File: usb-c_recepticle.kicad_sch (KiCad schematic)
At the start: 4 parts, among them J2 USB_C_Receptacle_USB2.0_16P, U7 USBLC6-2SC6

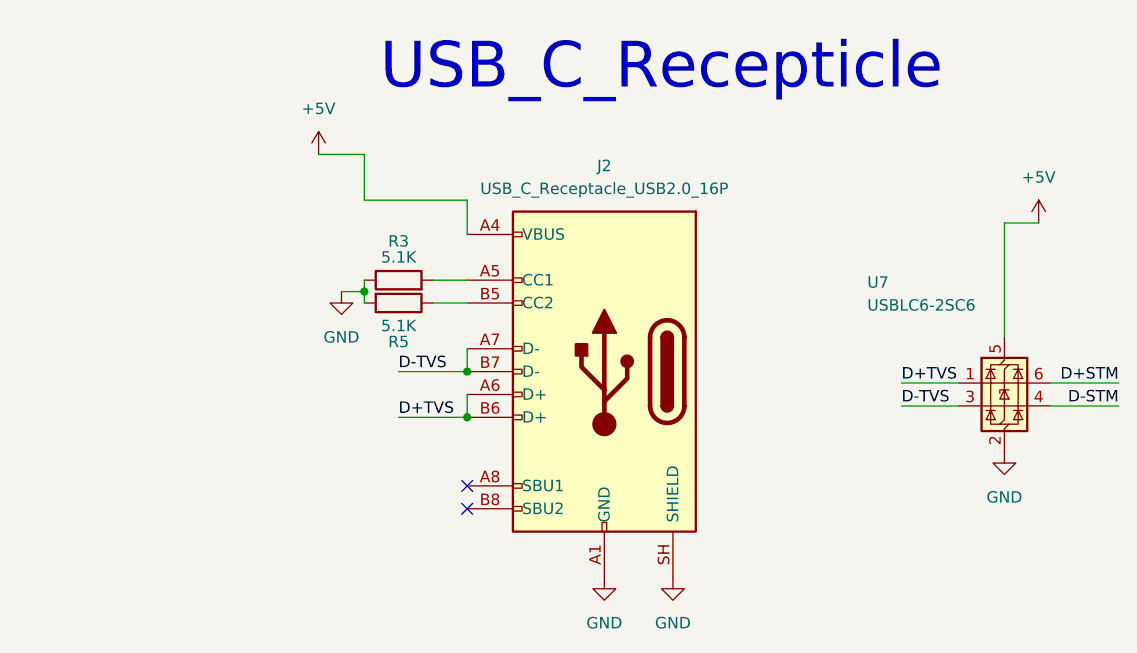
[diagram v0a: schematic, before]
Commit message: Feat: added Canbus
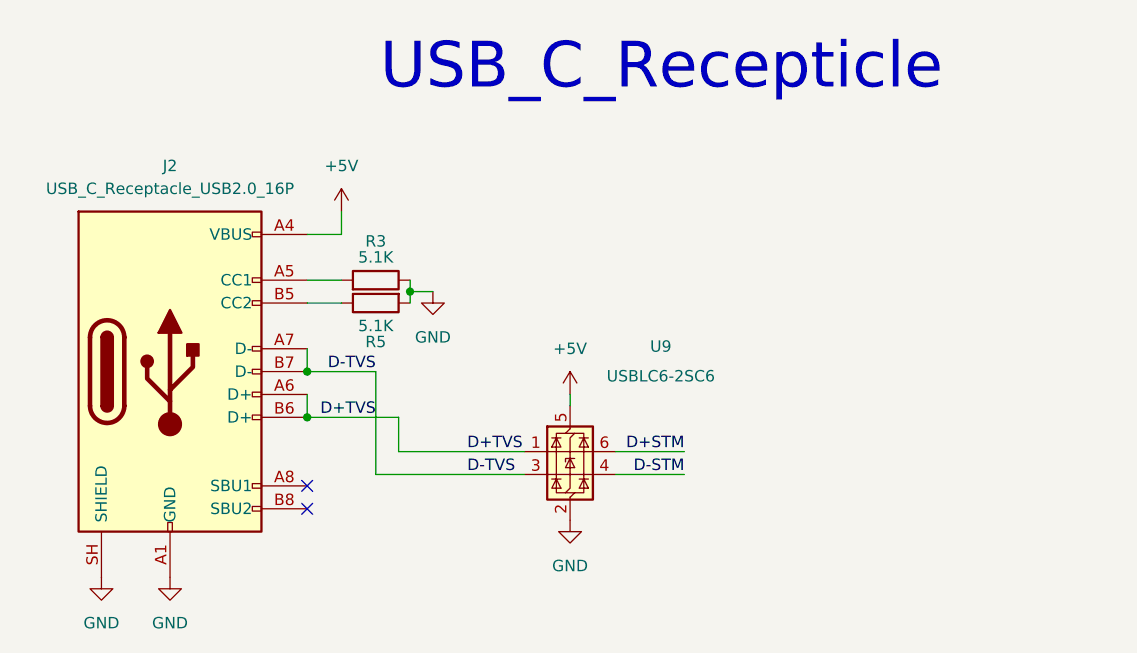
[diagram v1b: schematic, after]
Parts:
- removed U7: USBLC6-2SC6, Package_TO_SOT_SMD:SOT-23-6, symbol Power_Protection:USBLC6-2SC6
- added U9: USBLC6-2SC6, Package_TO_SOT_SMD:SOT-23-6, symbol Power_Protection:USBLC6-2SC6
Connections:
- net D-TVS is gone; now on net D+TVS: J2.A7 (D-), J2.B7 (D-)
- net +5V: now also U9.5 (VBUS)
- net D+STM: now also U9.6 (I/O1)
- net D+TVS: now also U9.1 (I/O1), U9.3 (I/O2)
- net D-STM: now also U9.4 (I/O2)
- net GND: now also U9.2 (GND)
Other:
- moved on the sheet: J2, R3, R5
